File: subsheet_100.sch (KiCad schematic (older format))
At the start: 21 parts, among them U100 MC68000_PLCC_68_PHY, U100_DIP64 MC68000_DIP_64_SOCKET

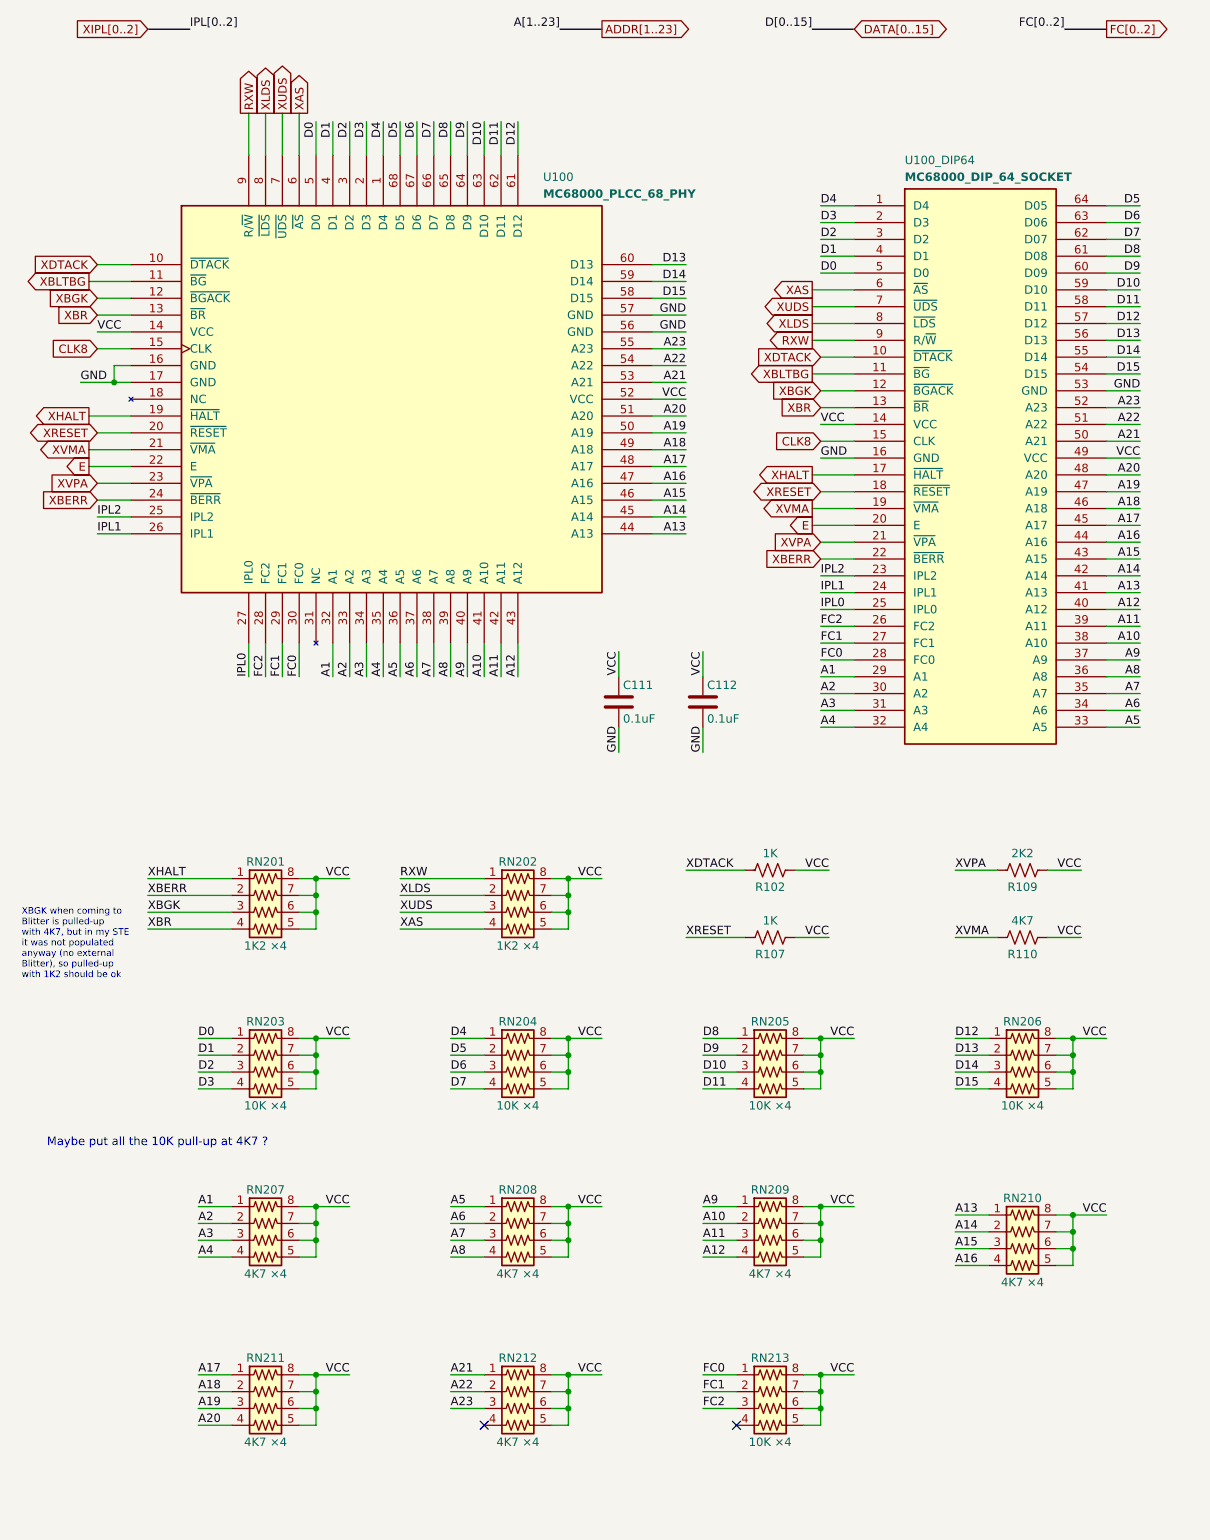
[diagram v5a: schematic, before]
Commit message: Resolves #2 : apply the pull-up fix to data and address bus
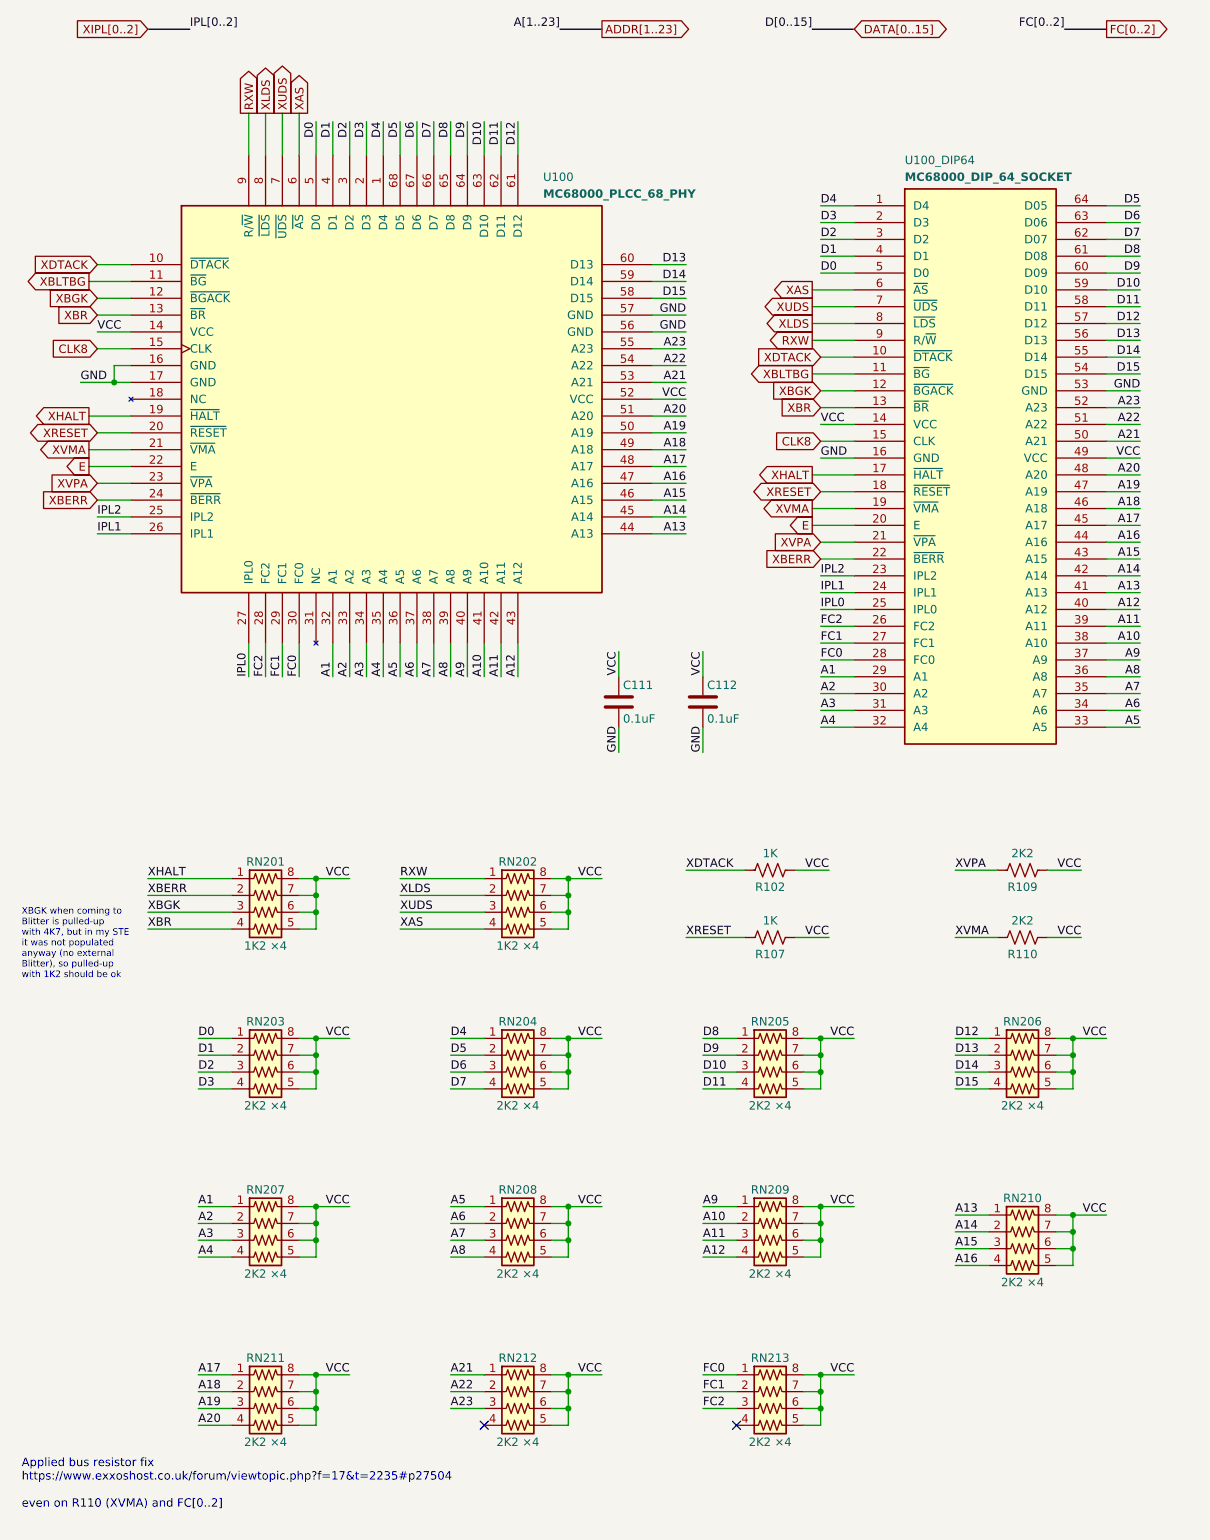
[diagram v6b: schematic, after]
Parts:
- R110: value 4K7 -> 2K2
- RN203, RN204, RN205, RN206, RN213: value 10K ×4 -> 2K2 ×4
- RN207, RN208, RN209, RN210, RN211, RN212: value 4K7 ×4 -> 2K2 ×4
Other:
- note added: "Applied bus resistor fix\nhttps://www.exxoshost.co.uk/forum/viewtopic.php?f=17&t=2235#p27504\n\neven on R110 (XVMA) and FC[0..2]"
- note removed: "Maybe put all the 10K pull-up at 4K7 ?"
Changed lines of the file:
@@
 P 6500 6400
 F 0 "R110" V 6600 6400 50  0000 C CNN
-F 1 "4K7" V 6400 6400 50  0000 C CNN
+F 1 "2K2" V 6400 6400 50  0000 C CNN
 F 2 "commons_passives_THT:Passive_THT_resistor_W2.54mm_L12.70mm" V 6540 6390 50  0001 C CNN
 F 3 "~" H 6500 6400 50  0001 C CNN
@@
 P 2000 7200
 F 0 "RN203" V 1700 7200 50  0000 C CNN
-F 1 "10K ×4" V 2200 7200 50  0000 C CNN
+F 1 "2K2 ×4" V 2200 7200 50  0000 C CNN
 F 2 "Resistor_SMD:R_Array_Convex_4x0603" V 2275 7200 50  0001 C CNN
 F 3 "~" H 2000 7200 50  0001 C CNN
@@
 P 3500 7200
 F 0 "RN204" V 3200 7200 50  0000 C CNN
-F 1 "10K ×4" V 3700 7200 50  0000 C CNN
+F 1 "2K2 ×4" V 3700 7200 50  0000 C CNN
 F 2 "Resistor_SMD:R_Array_Convex_4x0603" V 3775 7200 50  0001 C CNN
 F 3 "~" H 3500 7200 50  0001 C CNN
@@
 P 5000 7200
 F 0 "RN205" V 4700 7200 50  0000 C CNN
-F 1 "10K ×4" V 5200 7200 50  0000 C CNN
+F 1 "2K2 ×4" V 5200 7200 50  0000 C CNN
 F 2 "Resistor_SMD:R_Array_Convex_4x0603" V 5275 7200 50  0001 C CNN
 F 3 "~" H 5000 7200 50  0001 C CNN
@@
 P 6500 7200
 F 0 "RN206" V 6200 7200 50  0000 C CNN
-F 1 "10K ×4" V 6700 7200 50  0000 C CNN
+F 1 "2K2 ×4" V 6700 7200 50  0000 C CNN
 F 2 "Resistor_SMD:R_Array_Convex_4x0603" V 6775 7200 50  0001 C CNN
 F 3 "~" H 6500 7200 50  0001 C CNN
@@
 P 2000 8200
 F 0 "RN207" V 1700 8200 50  0000 C CNN
-F 1 "4K7 ×4" V 2200 8200 50  0000 C CNN
+F 1 "2K2 ×4" V 2200 8200 50  0000 C CNN
 F 2 "Resistor_SMD:R_Array_Convex_4x0603" V 2275 8200 50  0001 C CNN
 F 3 "~" H 2000 8200 50  0001 C CNN
@@
 P 3500 8200
 F 0 "RN208" V 3200 8200 50  0000 C CNN
-F 1 "4K7 ×4" V 3700 8200 50  0000 C CNN
+F 1 "2K2 ×4" V 3700 8200 50  0000 C CNN
 F 2 "Resistor_SMD:R_Array_Convex_4x0603" V 3775 8200 50  0001 C CNN
 F 3 "~" H 3500 8200 50  0001 C CNN
@@
 P 5000 8200
 F 0 "RN209" V 4700 8200 50  0000 C CNN
-F 1 "4K7 ×4" V 5200 8200 50  0000 C CNN
+F 1 "2K2 ×4" V 5200 8200 50  0000 C CNN
 F 2 "Resistor_SMD:R_Array_Convex_4x0603" V 5275 8200 50  0001 C CNN
 F 3 "~" H 5000 8200 50  0001 C CNN
@@
 P 6500 8250
 F 0 "RN210" V 6200 8250 50  0000 C CNN
-F 1 "4K7 ×4" V 6700 8250 50  0000 C CNN
+F 1 "2K2 ×4" V 6700 8250 50  0000 C CNN
 F 2 "Resistor_SMD:R_Array_Convex_4x0603" V 6775 8250 50  0001 C CNN
 F 3 "~" H 6500 8250 50  0001 C CNN
@@
 P 2000 9200
 F 0 "RN211" V 1700 9200 50  0000 C CNN
-F 1 "4K7 ×4" V 2200 9200 50  0000 C CNN
+F 1 "2K2 ×4" V 2200 9200 50  0000 C CNN
 F 2 "Resistor_SMD:R_Array_Convex_4x0603" V 2275 9200 50  0001 C CNN
 F 3 "~" H 2000 9200 50  0001 C CNN
@@
 P 3500 9200
 F 0 "RN212" V 3200 9200 50  0000 C CNN
-F 1 "4K7 ×4" V 3700 9200 50  0000 C CNN
+F 1 "2K2 ×4" V 3700 9200 50  0000 C CNN
 F 2 "Resistor_SMD:R_Array_Convex_4x0603" V 3775 9200 50  0001 C CNN
 F 3 "~" H 3500 9200 50  0001 C CNN
@@
 P 5000 9200
 F 0 "RN213" V 4700 9200 50  0000 C CNN
-F 1 "10K ×4" V 5200 9200 50  0000 C CNN
+F 1 "2K2 ×4" V 5200 9200 50  0000 C CNN
 F 2 "Resistor_SMD:R_Array_Convex_4x0603" V 5275 9200 50  0001 C CNN
 F 3 "~" H 5000 9200 50  0001 C CNN
@@
 Wire Wire Line
 	5300 9100 5300 9000
-Text Notes 700  7650 0    50   ~ 0
-Maybe put all the 10K pull-up at 4K7 ?
+Text Notes 550  9800 0    50   ~ 0
+Applied bus resistor fix\nhttps://www.exxoshost.co.uk/forum/viewtopic.php?f=17&t=2235#p27504\n\neven on R110 (XVMA) and FC[0..2]
 NoConn ~ 3300 9300
 NoConn ~ 4800 9300

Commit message: Resolves #13 : assign 1206 hand-solder footprints to resistors
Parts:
- R102, R107, R109, R110: footprint commons_passives_THT:Passive_THT_resistor_W2.54mm_L12.70mm -> Resistor_SMD:R_1206_3216Metric_Pad1.30x1.75mm_HandSolder
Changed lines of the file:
@@
 F 0 "R102" V 5100 6000 50  0000 C CNN
 F 1 "1K" V 4900 6000 50  0000 C CNN
-F 2 "commons_passives_THT:Passive_THT_resistor_W2.54mm_L12.70mm" V 5040 5990 50  0001 C CNN
+F 2 "Resistor_SMD:R_1206_3216Metric_Pad1.30x1.75mm_HandSolder" V 5040 5990 50  0001 C CNN
 F 3 "~" H 5000 6000 50  0001 C CNN
 	1    5000 6000
@@
 F 0 "R107" V 5100 6400 50  0000 C CNN
 F 1 "1K" V 4900 6400 50  0000 C CNN
-F 2 "commons_passives_THT:Passive_THT_resistor_W2.54mm_L12.70mm" V 5040 6390 50  0001 C CNN
+F 2 "Resistor_SMD:R_1206_3216Metric_Pad1.30x1.75mm_HandSolder" V 5040 6390 50  0001 C CNN
 F 3 "~" H 5000 6400 50  0001 C CNN
 	1    5000 6400
@@
 F 0 "R109" V 6600 6000 50  0000 C CNN
 F 1 "2K2" V 6400 6000 50  0000 C CNN
-F 2 "commons_passives_THT:Passive_THT_resistor_W2.54mm_L12.70mm" V 6540 5990 50  0001 C CNN
+F 2 "Resistor_SMD:R_1206_3216Metric_Pad1.30x1.75mm_HandSolder" V 6540 5990 50  0001 C CNN
 F 3 "~" H 6500 6000 50  0001 C CNN
 	1    6500 6000
@@
 F 0 "R110" V 6600 6400 50  0000 C CNN
 F 1 "2K2" V 6400 6400 50  0000 C CNN
-F 2 "commons_passives_THT:Passive_THT_resistor_W2.54mm_L12.70mm" V 6540 6390 50  0001 C CNN
+F 2 "Resistor_SMD:R_1206_3216Metric_Pad1.30x1.75mm_HandSolder" V 6540 6390 50  0001 C CNN
 F 3 "~" H 6500 6400 50  0001 C CNN
 	1    6500 6400
